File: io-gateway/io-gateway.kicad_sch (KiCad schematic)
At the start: 16 parts, among them IC1 MAX17673AATI+

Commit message: temp commit
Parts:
- added R10: 3K9, Resistor_SMD:R_0201_0603Metric, symbol Device:R
- added R11: 100R, Resistor_SMD:R_0201_0603Metric, symbol Device:R
- added R12: 470R, Resistor_SMD:R_0201_0603Metric, symbol Device:R
- added R13, R15: 22K, Resistor_SMD:R_0201_0603Metric, symbol Device:R
- added R14: 390K, Resistor_SMD:R_0201_0603Metric, symbol Device:R
- added R16: open, Resistor_SMD:R_0201_0603Metric, symbol Device:R
- added R17: 0R, Resistor_SMD:R_0201_0603Metric, symbol Device:R
- added R18, R19, R20: 100K, Resistor_SMD:R_0201_0603Metric, symbol Device:R
- added R5: 68K, Resistor_SMD:R_0201_0603Metric, symbol Device:R
- added R6: 180K, Resistor_SMD:R_0201_0603Metric, symbol Device:R
- added R7: 1K, Resistor_SMD:R_0201_0603Metric, symbol Device:R
- added R8: 12K, Resistor_SMD:R_0201_0603Metric, symbol Device:R
- added R9: 39K, Resistor_SMD:R_0201_0603Metric, symbol Device:R
- C2, C3, C6, C8: value C -> open
- R1: value R -> 12K
- R2: value R -> 8K2
- R3: value R -> 10K
- R4: value R -> 3K3
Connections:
- net +3V3: now also R14.1
- net +5V: now also R5.1
- net GND: now also IC1.27 (PGNDB), R10.2, R15.2, R16.2, R17.2
- net at IC1.7 (FBA), R3.2, R4.1: now also R14.2, R15.1
- net at IC1.13 (FBH): now also R7.2, R8.1
- net at IC1.2 (POKH): now also R18.2
- net at IC1.3 (POKB): now also R19.2
- net at IC1.4 (MODE/SYNC): now also R17.1
- net at IC1.5 (POKA): now also R20.2
- net at IC1.6 (RT): now also R16.1
- new net: R1.2, R11.1
- new net: IC1.1 (FBB), R11.2, R12.1, R13.1
- new net: R12.2, R13.2, R2.1
- new net: R8.2, R9.1
- new net: R10.1, R9.2
- new net: R6.2, R7.1
- new net: R5.2, R6.1
- new net +24V: R18.1, R19.1, R20.1
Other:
- moved on the sheet: C2, R1, R2, R3, R4

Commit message: buck regulator ready
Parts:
- removed R10: 3K9, Resistor_SMD:R_0201_0603Metric, symbol Device:R
- removed R13: 22K, Resistor_SMD:R_0201_0603Metric, symbol Device:R
- added C10, C13, C9: 2.2µF, Capacitor_SMD:C_0603_1608Metric, symbol Device:C
- added C11: 47µF, Capacitor_SMD:C_0603_1608Metric, symbol Device:C
- added C12: 1µF, Capacitor_SMD:C_0603_1608Metric, symbol Device:C
- added C14, C16, C20, C21: 100nF, Capacitor_SMD:C_0603_1608Metric, symbol Device:C
- added C15: 4.7µF, Capacitor_SMD:CP_Elec_4x5.4, symbol Device:C_Polarized
- added C17: open, Capacitor_SMD:C_0603_1608Metric, symbol Device:C
- added C18: 47µF, Capacitor_SMD:CP_Elec_6.3x5.4, symbol Device:C_Polarized
- added C19: 4.7µF, Capacitor_SMD:C_0603_1608Metric, symbol Device:C
- added JP1, JP2: Jumper_2_Bridged, TestPoint:TestPoint_2Pads_Pitch2.54mm_Drill0.8mm, symbol Jumper:Jumper_2_Bridged
- added R21: 0R, Resistor_SMD:R_0201_0603Metric, symbol Device:R
- R12: value 470R -> 10K
- R14: value 390K -> 470K
- R18, R19, R20: value 100K -> open
- R2: value 8K2 -> 68K
- R5: value 68K -> 330k
- R6: value 180K -> 1M
- R7: value 1K -> 1R
- R8: value 12K -> 22K
- R9: value 39K -> 33K
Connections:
- net +24V: now also IC1.15 (ENH), IC1.16 (INH), C15.1, C16.1, C17.1, C18.1, C19.1, C21.1; no longer R18.1, R19.1, R20.1
- net +5V: now also R6.1, R7.1, C11.1, JP1.2 (B), JP2.1 (A)
- net GND: now also IC1.17 (PGNDH), IC1.20 (GND), IC1.22 (SGND), IC1.9 (PGNDA), R12.2, R9.2, C10.1, C11.2, C12.2, C13.2, C15.2, C16.2, C17.2, C18.2, C19.2, C20.2, C21.2, C9.2, R21.2
- net at IC1.1 (FBB), R11.2, R12.1: now also R2.1
- net at IC1.18 (LXH), L2.1: now also C14.2
- net at IC1.10 (INA): now also IC1.11 (ENA), C10.2, JP2.2 (B)
- net SSH: now reaches IC1.12 (SSH)
- net SSH: now also C20.1
- net at IC1.13 (FBH), R8.1: now also R5.2, R6.2; no longer R7.2
- net at IC1.19 (BSTH): now also C14.1
- net MX_VCC: now reaches IC1.21 (VCC)
- net MX_VCC: now also R18.1, R19.1, R20.1, C13.1
- net MX_EXTVCC: now reaches IC1.23 (EXTVCC)
- net at IC1.24 (FDIV): now also R21.1
- net at IC1.25 (ENB): now also IC1.26 (INB), C9.1, JP1.1 (A)
- new net EXTVCC: C12.1, R7.2
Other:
- moved on the sheet: C5, C6, C7, C8, L2, L3, R2, R5, R8, R9

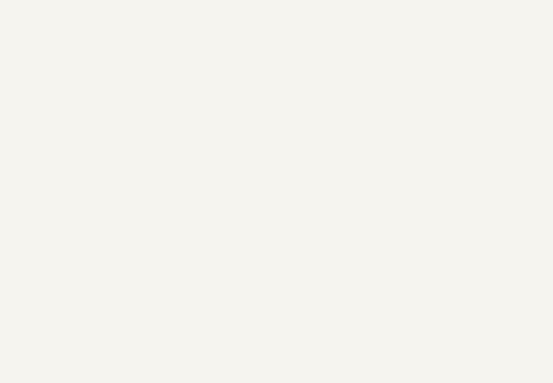
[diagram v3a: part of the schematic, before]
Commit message: add Terminal Blocks
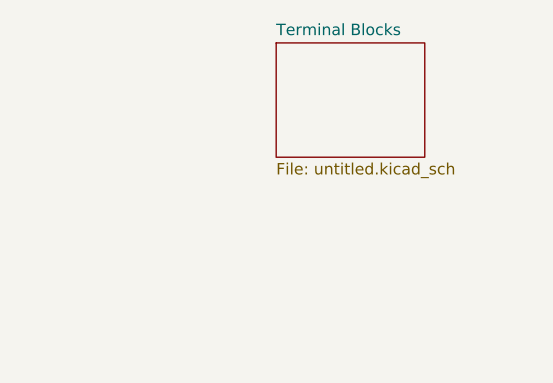
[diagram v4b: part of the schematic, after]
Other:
- added sheet Terminal Blocks (untitled.kicad_sch)
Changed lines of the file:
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@@
+		)
+	)
+	(sheet
+		(at 302.26 1.27)
+		(size 16.51 12.7)
+		(exclude_from_sim no)
+		(in_bom yes)
+		(on_board yes)
+		(dnp no)
+		(fields_autoplaced yes)
+		(stroke
+			(width 0.1524)
+			(type solid)
+		)
+		(fill
+			(color 0 0 0 0.0000)
+		)
+		(property "Sheetname" "Terminal Blocks"
+			(at 302.26 0.5584 0)
+			(effects
+				(font
+					(size 1.27 1.27)
+				)
+				(justify left bottom)
+			)
+		)
+		(property "Sheetfile" "untitled.kicad_sch"
+			(at 302.26 14.5546 0)
+			(effects
+				(font
+					(size 1.27 1.27)
+				)
+				(justify left top)
+			)
+		)
+		(instances
+			(project "io-gateway"
+				(path "/2cb6f94b-272a-4ed7-b08d-c3630bda6156"
+					(page "2")
+				)
+			)
 		)
 	)

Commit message: add relays
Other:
- added sheet FRDM-MCXN947 (FRDM-MCXN947.kicad_sch)
- added sheet RelaysJ4 (relays.kicad_sch)
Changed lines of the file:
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@@
+		)
+	)
+	(sheet
+		(at 303.53 22.86)
+		(size 15.24 11.43)
+		(exclude_from_sim no)
+		(in_bom yes)
+		(on_board yes)
+		(dnp no)
+		(fields_autoplaced yes)
+		(stroke
+			(width 0.1524)
+			(type solid)
+		)
+		(fill
+			(color 0 0 0 0.0000)
+		)
+		(property "Sheetname" "RelaysJ4"
+			(at 303.53 22.1484 0)
+			(effects
+				(font
+					(size 1.27 1.27)
+				)
+				(justify left bottom)
+			)
+		)
+		(property "Sheetfile" "relays.kicad_sch"
+			(at 303.53 34.8746 0)
+			(effects
+				(font
+					(size 1.27 1.27)
+				)
+				(justify left top)
+			)
+		)
+		(instances
+			(project "io-gateway"
+				(path "/2cb6f94b-272a-4ed7-b08d-c3630bda6156"
+					(page "3")
+				)
+			)
+		)
+	)
+	(sheet
+		(at 303.53 43.18)
+		(size 12.7 7.62)
+		(exclude_from_sim no)
+		(in_bom yes)
+		(on_board yes)
+		(dnp no)
+		(fields_autoplaced yes)
+		(stroke
+			(width 0.1524)
+			(type solid)
+		)
+		(fill
+			(color 0 0 0 0.0000)
+		)
+		(property "Sheetname" "FRDM-MCXN947"
+			(at 303.53 42.4684 0)
+			(effects
+				(font
+					(size 1.27 1.27)
+				)
+				(justify left bottom)
+			)
+		)
+		(property "Sheetfile" "FRDM-MCXN947.kicad_sch"
+			(at 303.53 51.3846 0)
+			(effects
+				(font
+					(size 1.27 1.27)
+				)
+				(justify left top)
+			)
+		)
+		(instances
+			(project "io-gateway"
+				(path "/2cb6f94b-272a-4ed7-b08d-c3630bda6156"
+					(page "4")
+				)
+			)
 		)
 	)

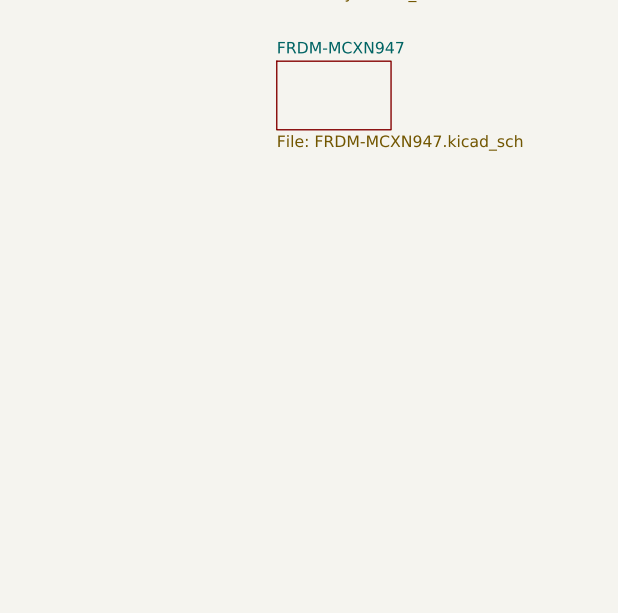
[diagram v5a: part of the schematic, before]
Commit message: Place Relays
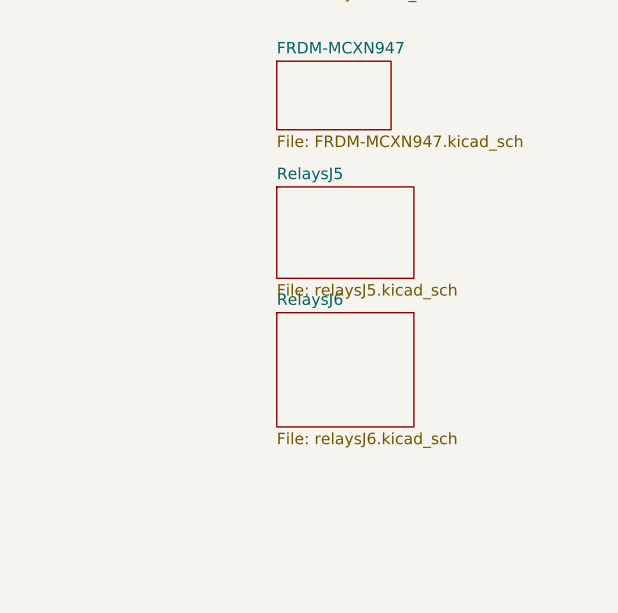
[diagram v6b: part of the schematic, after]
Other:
- added sheet RelaysJ5 (relaysJ5.kicad_sch)
- added sheet RelaysJ6 (relaysJ6.kicad_sch)
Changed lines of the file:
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@@
+	)
+	(sheet
+		(at 303.53 71.12)
+		(size 15.24 12.7)
+		(exclude_from_sim no)
+		(in_bom yes)
+		(on_board yes)
+		(dnp no)
+		(fields_autoplaced yes)
+		(stroke
+			(width 0.1524)
+			(type solid)
+		)
+		(fill
+			(color 0 0 0 0.0000)
+		)
+		(property "Sheetname" "RelaysJ6"
+			(at 303.53 70.4084 0)
+			(effects
+				(font
+					(size 1.27 1.27)
+				)
+				(justify left bottom)
+			)
+		)
+		(property "Sheetfile" "relaysJ6.kicad_sch"
+			(at 303.53 84.4046 0)
+			(effects
+				(font
+					(size 1.27 1.27)
+				)
+				(justify left top)
+			)
+		)
+		(instances
+			(project "io-gateway"
+				(path "/2cb6f94b-272a-4ed7-b08d-c3630bda6156"
+					(page "6")
+				)
+			)
+		)
 	)
 	(sheet
@@
 			(project "io-gateway"
 				(path "/2cb6f94b-272a-4ed7-b08d-c3630bda6156"
-					(page "2")
+					(page "3")
+				)
+			)
+		)
+	)
+	(sheet
+		(at 303.53 57.15)
+		(size 15.24 10.16)
+		(exclude_from_sim no)
+		(in_bom yes)
+		(on_board yes)
+		(dnp no)
+		(fields_autoplaced yes)
+		(stroke
+			(width 0.1524)
+			(type solid)
+		)
+		(fill
+			(color 0 0 0 0.0000)
+		)
+		(property "Sheetname" "RelaysJ5"
+			(at 303.53 56.4384 0)
+			(effects
+				(font
+					(size 1.27 1.27)
+				)
+				(justify left bottom)
+			)
+		)
+		(property "Sheetfile" "relaysJ5.kicad_sch"
+			(at 303.53 67.8946 0)
+			(effects
+				(font
+					(size 1.27 1.27)
+				)
+				(justify left top)
+			)
+		)
+		(instances
+			(project "io-gateway"
+				(path "/2cb6f94b-272a-4ed7-b08d-c3630bda6156"
+					(page "5")
 				)
 			)
@@
 			(project "io-gateway"
 				(path "/2cb6f94b-272a-4ed7-b08d-c3630bda6156"
-					(page "3")
+					(page "4")
 				)
 			)
@@
 			(project "io-gateway"
 				(path "/2cb6f94b-272a-4ed7-b08d-c3630bda6156"
-					(page "4")
-				)
-			)
+					(page "2")
+				)
+			)

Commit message: add dimmer
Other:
- added sheet Dimmer1 (dimmer1.kicad_sch)
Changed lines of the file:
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@@
+	)
+	(sheet
+		(at 303.53 92.71)
+		(size 19.05 17.78)
+		(exclude_from_sim no)
+		(in_bom yes)
+		(on_board yes)
+		(dnp no)
+		(fields_autoplaced yes)
+		(stroke
+			(width 0.1524)
+			(type solid)
+		)
+		(fill
+			(color 0 0 0 0.0000)
+		)
+		(property "Sheetname" "Dimmer1"
+			(at 303.53 91.9984 0)
+			(effects
+				(font
+					(size 1.27 1.27)
+				)
+				(justify left bottom)
+			)
+		)
+		(property "Sheetfile" "dimmer1.kicad_sch"
+			(at 303.53 111.0746 0)
+			(effects
+				(font
+					(size 1.27 1.27)
+				)
+				(justify left top)
+			)
+		)
+		(instances
+			(project "io-gateway"
+				(path "/2cb6f94b-272a-4ed7-b08d-c3630bda6156"
+					(page "7")
+				)
+			)
+		)
 	)
 	(sheet

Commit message: layout for first dimmer
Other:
- moved on the sheet: L2
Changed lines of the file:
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@@
+	(wire
+		(pts
+			(xy 158.75 74.93) (xy 157.48 74.93)
+		)
+		(stroke
+			(width 0)
+			(type default)
+		)
+	)
 	(wire
 		(pts
@@
 	(wire
 		(pts
-			(xy 165.1 74.93) (xy 170.18 74.93)
+			(xy 166.37 74.93) (xy 170.18 74.93)
 		)
 		(stroke
@@
 	(symbol
 		(lib_id "Device:L")
-		(at 161.29 74.93 90)
+		(at 162.56 74.93 90)
 		(unit 1)
 		(exclude_from_sim no)
@@
 		(fields_autoplaced yes)
 		(property "Reference" "L2"
-			(at 161.29 69.85 90)
+			(at 162.56 69.85 90)
 			(effects
 				(font
@@
 		)
 		(property "Value" "22µH"
-			(at 161.29 72.39 90)
+			(at 162.56 72.39 90)
 			(effects
 				(font
@@
 		)
 		(property "Footprint" "Inductor_SMD:L_1008_2520Metric"
-			(at 161.29 74.93 0)
+			(at 162.56 74.93 0)
 			(effects
 				(font
@@
 		)
 		(property "Datasheet" "~"
-			(at 161.29 74.93 0)
+			(at 162.56 74.93 0)
 			(effects
 				(font
@@
 		)
 		(property "Description" "Inductor"
-			(at 161.29 74.93 0)
-			(effects
-				(font
+			(at 162.56 74.93 0)
+			(effects
+				(font
